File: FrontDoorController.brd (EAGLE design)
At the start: 31.4 x 52.1 mm, 2 parts

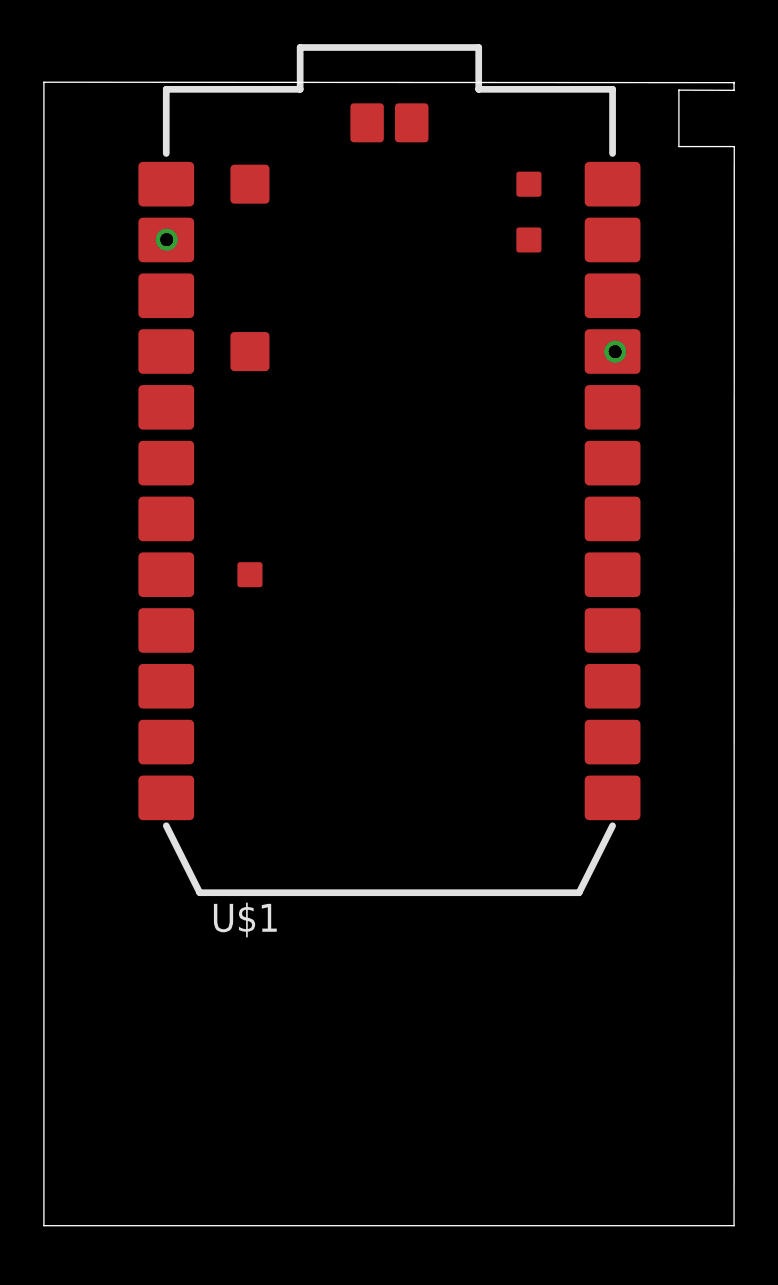
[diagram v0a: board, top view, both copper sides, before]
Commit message: Door_Control_PCB: Add motor driver and connect
Add the TB6612FNG motor driver and connect it to the Photon.  This will
take power from 4 AA batteries in the Lockitron and drive the Lockitron
motor.  The Photon will control direction and speed for the motor.
Since there is only 1 motor on the Lockitron, only 1 of the input/output
pairs on the driver needs to be connected.
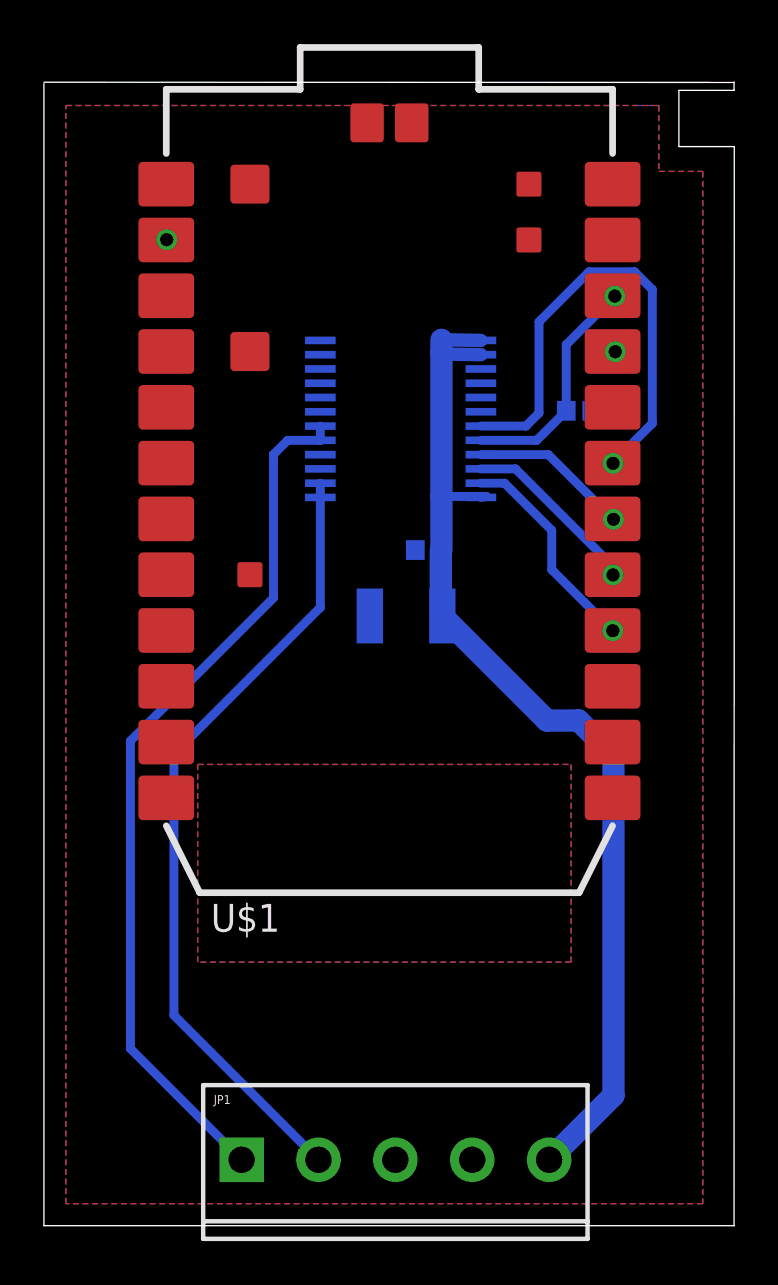
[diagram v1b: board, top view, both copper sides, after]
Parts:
- added C1: 10uf, SparkFun-Capacitors:EIA3528
- added C2, C3: 0.1uf, SparkFun-Capacitors:0402-CAP
- added JP1: (no value), SparkFun-Connectors:SCREWTERMINAL-3.5MM-5
- added U$2: TB6612FNG, SparkFun-PowerIC:SSOP24
- moved FRAME1 78.2 mm to (87.0, 34.0)
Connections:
- net RST_B renamed RSTB
- net SETUP_B renamed SETUPB
- removed net D3: U$1.16
- removed net D4: U$1.17
- removed net D5: U$1.18
- removed net D6: U$1.19
- removed net VBAT: U$1.22
- new net A01: JP1.2, U$2.1, U$2.2
- new net A02: JP1.1, U$2.5, U$2.6
- new net AIN1: U$1.18, U$2.21
- new net AIN2: U$1.17, U$2.22
- new net PWMA: U$1.16, U$2.23
- new net STBY: U$1.19, U$2.19
- new net VM: C1.A, C2.1, JP1.5, U$2.13, U$2.14, U$2.24
- net 3V3: now also C3.1, U$1.22, U$2.20
- net GND: now also C1.C, C2.2, C3.2, JP1.3, JP1.4, U$2.10, U$2.18, U$2.3, U$2.4, U$2.9
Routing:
- net VM: track 0.00 -> 48.6 mm
- net A02: track 0.00 -> 40.0 mm
- net A01: track 0.00 -> 36.3 mm
- net STBY: track 0.00 -> 22.2 mm, vias 0 -> 1
- net 3V3: track 0.00 -> 10.7 mm, vias 0 -> 1
- net PWMA: track 0.00 -> 9.82 mm, vias 0 -> 1
- net AIN2: track 0.00 -> 8.26 mm, vias 0 -> 1
- net AIN1: track 0.00 -> 7.25 mm, vias 0 -> 1
- net GND: track 0.00 -> 0.16 mm, vias 0 -> 2
- added copper zone on layer 1, net 3V3
- added copper zone on layer 16, net GND
- added copper zone on layer 1, net N$3
- added copper zone on layer 16, net N$4
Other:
- outline, holes or cut-outs redrawn
- board text added: "A01"
- board text added: "A02"
- board text added: "AAin"
- board text added: "GND"

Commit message: Door_Control_PCB: Add headers and diode
Exchange the screw terminals for 0.1" breakaway header holes.  There is
no room for the screw terminals in the Lockitron so wires will need to
be soldered directly to the board.  Some space can be saved by using
0.1" spacing header holes instead of the bigger pitch screw terminals.
Also do a few other minor cleanup tasks like change the size of the wire
input labels.  Also add a 1N4001 diode between VM from AA's and VIN on
Photon to drop the voltage from about 6V to about 5V to ensure it is
safe for the Photon VIN input.
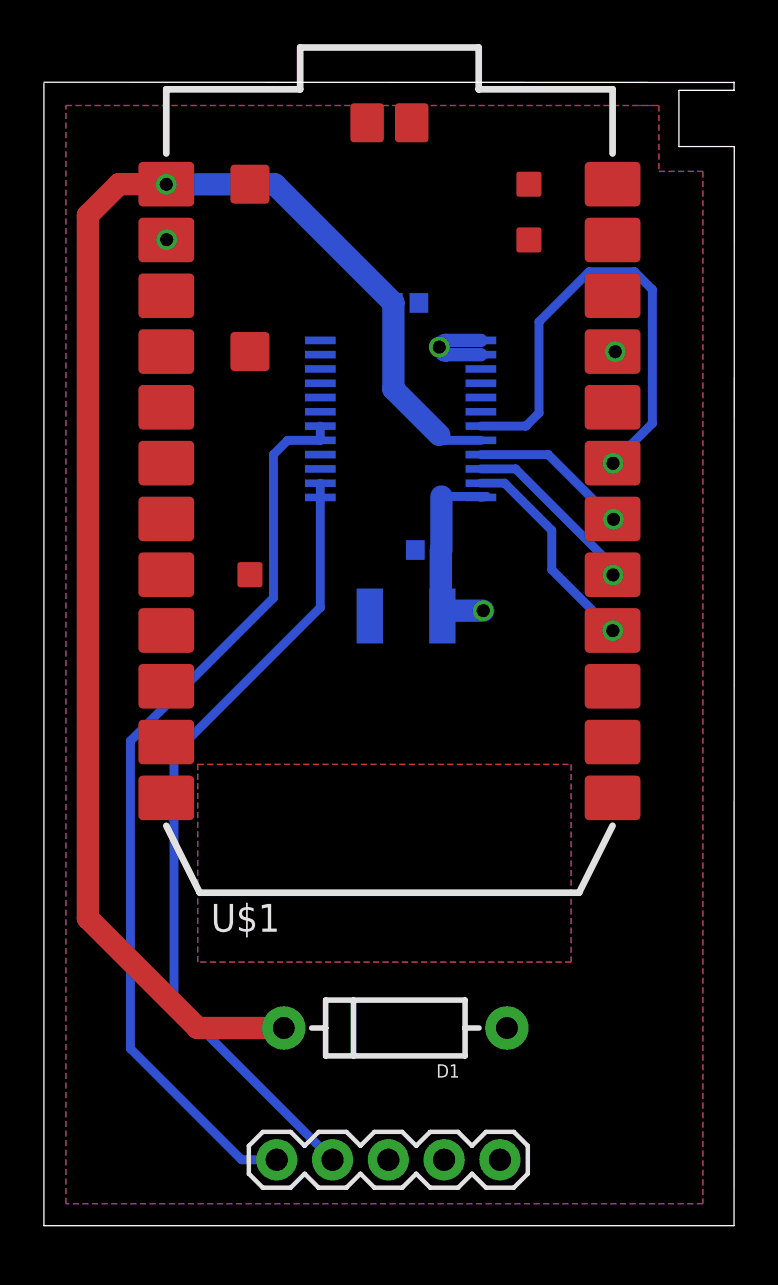
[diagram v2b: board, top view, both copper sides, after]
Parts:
- added D1: (no value), SparkFun-DiscreteSemi:DIODE-1N4001
- JP1: device SparkFun-Connectors:SCREWTERMINAL-3.5MM-5 -> SparkFun-Connectors:1X05
- moved C3 9.28 mm to (16.5, 42.0)
- moved JP1 1.60 mm to (10.6, 3.00)
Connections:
- new net VBAT: U$1.22
- net 3V3: no longer C3.1, U$1.22, U$2.20
- net VIN: now also C3.1, D1.C, U$2.20
- net VM: now also D1.A
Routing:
- net VIN: track 0.00 -> 68.6 mm, vias 0 -> 1
- net VM: track 48.6 -> 14.2 mm, vias 0 -> 2
- net 3V3: track 10.7 -> 0.00 mm, vias 1 -> 0
- net A02: track 40.0 -> 41.6 mm
- added copper zone on layer 1, net VM
- removed copper zone on layer 1, net 3V3
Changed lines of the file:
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@@
 <dimension x1="31.42" y1="51.69" x2="28.91" y2="51.7" x3="30.173240625" y3="53.763453125" textsize="1.778" layer="48" unit="inch"/>
 <dimension x1="31.42" y1="51.69" x2="31.43" y2="49.13" x3="39.882878125" y3="50.4430375" textsize="1.778" layer="48" unit="inch"/>
-<text x="10" y="7" size="1.778" layer="51" rot="R90">A02</text>
-<text x="13" y="7" size="1.778" layer="51" rot="R90">A01</text>
-<text x="15" y="7" size="1.778" layer="51">GND</text>
-<text x="24" y="7" size="1.778" layer="51" rot="R90">AAin</text>
+<text x="11" y="5" size="1.016" layer="51" rot="R90">A02</text>
+<text x="14" y="5" size="1.016" layer="51" rot="R90">A01</text>
+<text x="15.06" y="5" size="1.27" layer="51">GND</text>
+<text x="21" y="5" size="0.8128" layer="51" rot="R90">AAin</text>
 <wire x1="0" y1="0" x2="0" y2="52" width="0" layer="20"/>
 </plain>
@@
 <attribute name="NAME" x="17.719" y="31.5885" size="0.4064" layer="26" rot="MR0"/>
 </element>
-<element name="C3" library="SparkFun-Capacitors" package="0402-CAP" value="0.1uf" x="24.36" y="37.1" smashed="yes" rot="MR180">
-<attribute name="NAME" x="24.161" y="38.2315" size="0.4064" layer="26" rot="MR180"/>
+<element name="C3" library="SparkFun-Capacitors" package="0402-CAP" value="0.1uf" x="16.49" y="42.01" smashed="yes" rot="MR180">
+<attribute name="NAME" x="16.291" y="43.1415" size="0.4064" layer="26" rot="MR180"/>
 </element>
-<element name="JP1" library="SparkFun-Connectors" package="SCREWTERMINAL-3.5MM-5" value="" x="9" y="3">
-<attribute name="PROD_ID" value="Combine 8288+8399" x="9" y="3" size="1.778" layer="27" display="off"/>
+<element name="JP1" library="SparkFun-Connectors" package="1X05" value="" x="10.6" y="3" smashed="yes">
+<attribute name="VALUE" x="9.33" y="-0.175" size="1.27" layer="27"/>
 </element>
+<element name="D1" library="SparkFun-DiscreteSemi" package="DIODE-1N4001" value="" x="16" y="9" rot="R180"/>
 </elements>
 <signals>
 <signal name="VIN">
 <contactref element="U$1" pad="1"/>
+<contactref element="D1" pad="C"/>
+<wire x1="10.92" y1="9" x2="7" y2="9" width="1.016" layer="1"/>
+<wire x1="7" y1="9" x2="2" y2="14" width="1.016" layer="1"/>
+<wire x1="2" y1="14" x2="2" y2="46" width="1.016" layer="1"/>
+<wire x1="2" y1="46" x2="3.418" y2="47.418" width="1.016" layer="1"/>
+<wire x1="3.418" y1="47.418" x2="5.57" y2="47.418" width="1.016" layer="1"/>
+<contactref element="C3" pad="1"/>
+<contactref element="U$2" pad="20"/>
+<wire x1="15.91" y1="42.01" x2="15.91" y2="38.09" width="1.016" layer="16"/>
+<wire x1="15.91" y1="38.09" x2="18" y2="36" width="1.016" layer="16"/>
+<wire x1="18" y1="36" x2="18.245" y2="35.755" width="0.4064" layer="16"/>
+<wire x1="18.245" y1="35.755" x2="19.896" y2="35.755" width="0.4064" layer="16"/>
+<via x="5.57" y="47.41" extent="1-16" drill="0.6" shape="square"/>
+<wire x1="5.57" y1="47.41" x2="10.51" y2="47.41" width="1.016" layer="16"/>
+<wire x1="10.51" y1="47.41" x2="15.91" y2="42.01" width="1.016" layer="16"/>
+<wire x1="5.57" y1="47.418" x2="5.57" y2="47.41" width="0" layer="19" extent="1-1"/>
 </signal>
 <signal name="GND">
@@
 <signal name="3V3">
 <contactref element="U$1" pad="24"/>
-<contactref element="U$2" pad="20"/>
-<contactref element="U$1" pad="22"/>
-<contactref element="C3" pad="1"/>
-<polygon width="0.4064" layer="1">
-<vertex x="1" y="51"/>
-<vertex x="28" y="51"/>
-<vertex x="28" y="48"/>
-<vertex x="30" y="48"/>
-<vertex x="30" y="1"/>
-<vertex x="1" y="1"/>
-</polygon>
-<via x="25.99" y="42.32" extent="1-16" drill="0.6" shape="square"/>
-<wire x1="25.89" y1="42.338" x2="25.972" y2="42.338" width="0.4064" layer="16"/>
-<wire x1="25.972" y1="42.338" x2="25.99" y2="42.32" width="0.4064" layer="16"/>
-<wire x1="19.896" y1="35.755" x2="22.435" y2="35.755" width="0.4064" layer="16"/>
-<wire x1="22.435" y1="35.755" x2="23.78" y2="37.1" width="0.4064" layer="16"/>
-<wire x1="23.78" y1="37.1" x2="23.78" y2="40.11" width="0.4064" layer="16"/>
-<wire x1="23.78" y1="40.11" x2="25.99" y2="42.32" width="0.4064" layer="16"/>
 </signal>
 <signal name="RSTB">
@@
 <wire x1="12.584" y1="33.155" x2="12.584" y2="28.144" width="0.4064" layer="16"/>
 <wire x1="12.584" y1="28.144" x2="5.92" y2="21.48" width="0.4064" layer="16"/>
-<wire x1="5.92" y1="21.48" x2="5.92" y2="9.58" width="0.4064" layer="16"/>
-<wire x1="5.92" y1="9.58" x2="12.5" y2="3" width="0.4064" layer="16"/>
+<wire x1="13.14" y1="3" x2="5.92" y2="10.22" width="0.4064" layer="16"/>
+<wire x1="5.92" y1="10.22" x2="5.92" y2="21.48" width="0.4064" layer="16"/>
 </signal>
 <signal name="A02">
@@
 <wire x1="10.45" y1="28.58" x2="3.94" y2="22.07" width="0.4064" layer="16"/>
 <wire x1="3.94" y1="22.07" x2="3.94" y2="8.06" width="0.4064" layer="16"/>
-<wire x1="3.94" y1="8.06" x2="9" y2="3" width="0.4064" layer="16"/>
+<wire x1="10.6" y1="3" x2="9" y2="3" width="0.4064" layer="16"/>
+<wire x1="9" y1="3" x2="3.94" y2="8.06" width="0.4064" layer="16"/>
 </signal>
 <signal name="VM">
@@
 <wire x1="18.1" y1="33.2" x2="20.146" y2="33.2" width="0.4064" layer="16"/>
 <wire x1="20.146" y1="33.2" x2="19.896" y2="33.155" width="0.4064" layer="16"/>
-<wire x1="19.896" y1="40.305" x2="18.1" y2="40.335" width="0.6096" layer="16"/>
-<wire x1="18.1" y1="40.335" x2="18.1" y2="39.76" width="1.016" layer="16"/>
-<wire x1="18.1" y1="39.685" x2="18.1" y2="33.2" width="1.016" layer="16"/>
-<wire x1="19.896" y1="39.655" x2="18.1" y2="39.685" width="0.6096" layer="16"/>
 <wire x1="18.1" y1="39.685" x2="18.1" y2="39.76" width="0.4064" layer="16"/>
-<wire x1="18.14" y1="27.76" x2="22.9" y2="23" width="1.016" layer="16"/>
-<wire x1="22.9" y1="23" x2="24.34" y2="23" width="1.016" layer="16"/>
-<wire x1="24.34" y1="23" x2="25.93" y2="21.41" width="1.016" layer="16"/>
-<wire x1="25.93" y1="21.41" x2="25.93" y2="5.93" width="1.016" layer="16"/>
-<wire x1="25.93" y1="5.93" x2="23" y2="3" width="1.016" layer="16"/>
+<contactref element="D1" pad="A"/>
+<polygon width="0.4064" layer="1">
+<vertex x="1" y="51"/>
+<vertex x="28" y="51"/>
+<vertex x="28" y="48"/>
+<vertex x="30" y="48"/>
+<vertex x="30" y="1"/>
+<vertex x="1" y="1"/>
+</polygon>
+<wire x1="18.14" y1="27.76" x2="18.38" y2="28" width="1.016" layer="16"/>
+<wire x1="18.38" y1="28" x2="20" y2="28" width="1.016" layer="16"/>
+<via x="20" y="28" extent="1-16" drill="0.6"/>
+<via x="18" y="40" extent="1-16" drill="0.6"/>
+<wire x1="19.896" y1="40.305" x2="18.305" y2="40.305" width="0.6096" layer="16"/>
+<wire x1="18.305" y1="40.305" x2="18" y2="40" width="0.6096" layer="16" curve="90"/>
+<wire x1="19.896" y1="39.655" x2="18.345" y2="39.655" width="0.6096" layer="16"/>
+<wire x1="18.345" y1="39.655" x2="18" y2="40" width="0.6096" layer="16" curve="-90"/>
+<wire x1="18.345" y1="39.655" x2="18.205" y2="39.655" width="0.6096" layer="16"/>
+<wire x1="18.205" y1="39.655" x2="18.1" y2="39.76" width="0.6096" layer="16" curve="-90"/>
 </signal>
 <signal name="N$3">
@@
 <wire x1="25.89" y1="29.638" x2="25.89" y2="29.638" width="0" layer="19" extent="1-16"/>
 </signal>
+<signal name="VBAT">
+<contactref element="U$1" pad="22"/>
+</signal>
 </signals>

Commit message: Door_Control_PCB: Add Photon through holes
Add in an additional part for the Photon through-hole connections.  This
can be used to attach the Photon to the board without soldering it down.
Also reconnect the wires to the new Photon holes and clean up the
schematic a bit.
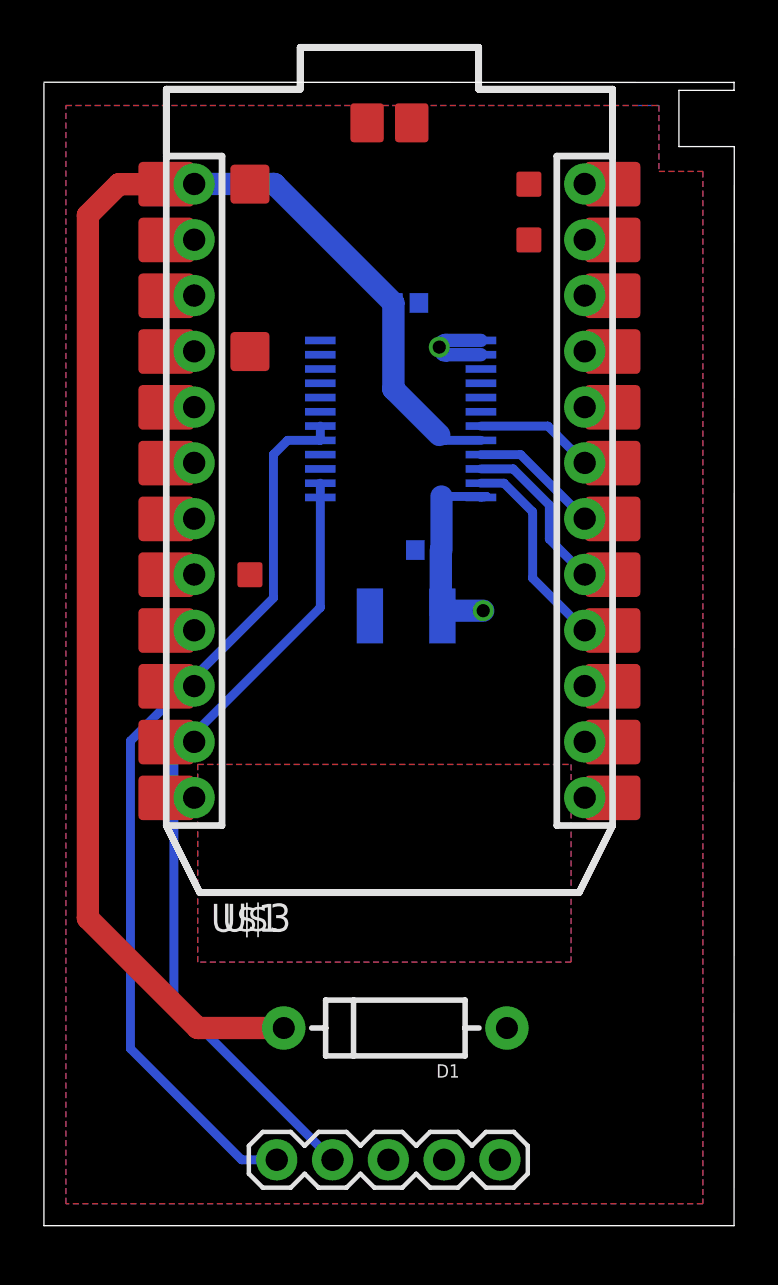
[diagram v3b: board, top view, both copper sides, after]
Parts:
- added U$3: PHOTON_WITH_HEADERS, Spark:PHOTON
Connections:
- net 3V3: now also U$3.24
- net A0: now also U$3.12
- net A1: now also U$3.11
- net A2: now also U$3.10
- net A3: now also U$3.9
- net A4: now also U$3.8
- net A5: now also U$3.7
- net AIN1: now also U$3.18
- net AIN2: now also U$3.17
- net D0: now also U$3.13
- net D1: now also U$3.14
- net D2: now also U$3.15
- net D7: now also U$3.20
- net DAC: now also U$3.6
- net GND: now also U$3.2, U$3.21
- net PWMA: now also U$3.16
- net RSTB: now also U$3.23
- net RX: now also U$3.4
- net STBY: now also U$3.19
- net TX: now also U$3.3
- net VBAT: now also U$3.22
- net VIN: now also U$3.1
- net WKP: now also U$3.5
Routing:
- net STBY: track 22.2 -> 6.69 mm, vias 1 -> 0
- net GND: track 0.16 -> 2.69 mm, vias 2 -> 0
- net A5: track 0.00 -> 1.27 mm
- net A3: track 0.00 -> 1.27 mm
- net A2: track 0.00 -> 1.27 mm
- net D2: track 0.00 -> 1.27 mm
- net VBAT: track 0.00 -> 1.27 mm
- net RSTB: track 0.00 -> 1.27 mm
- net D7: track 0.00 -> 1.27 mm
- net 3V3: track 0.00 -> 1.27 mm
- net WKP: track 0.00 -> 1.27 mm
- net TX: track 0.00 -> 1.27 mm
- net RX: track 0.00 -> 1.27 mm
- net DAC: track 0.00 -> 1.27 mm
- net A4: track 0.00 -> 1.27 mm
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
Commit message: Door_Control_PCB: Shrink the board a bit to save money
The board did not need to be nearly as big as it was and shrinking it a
bit can save some money in maunfacturing.
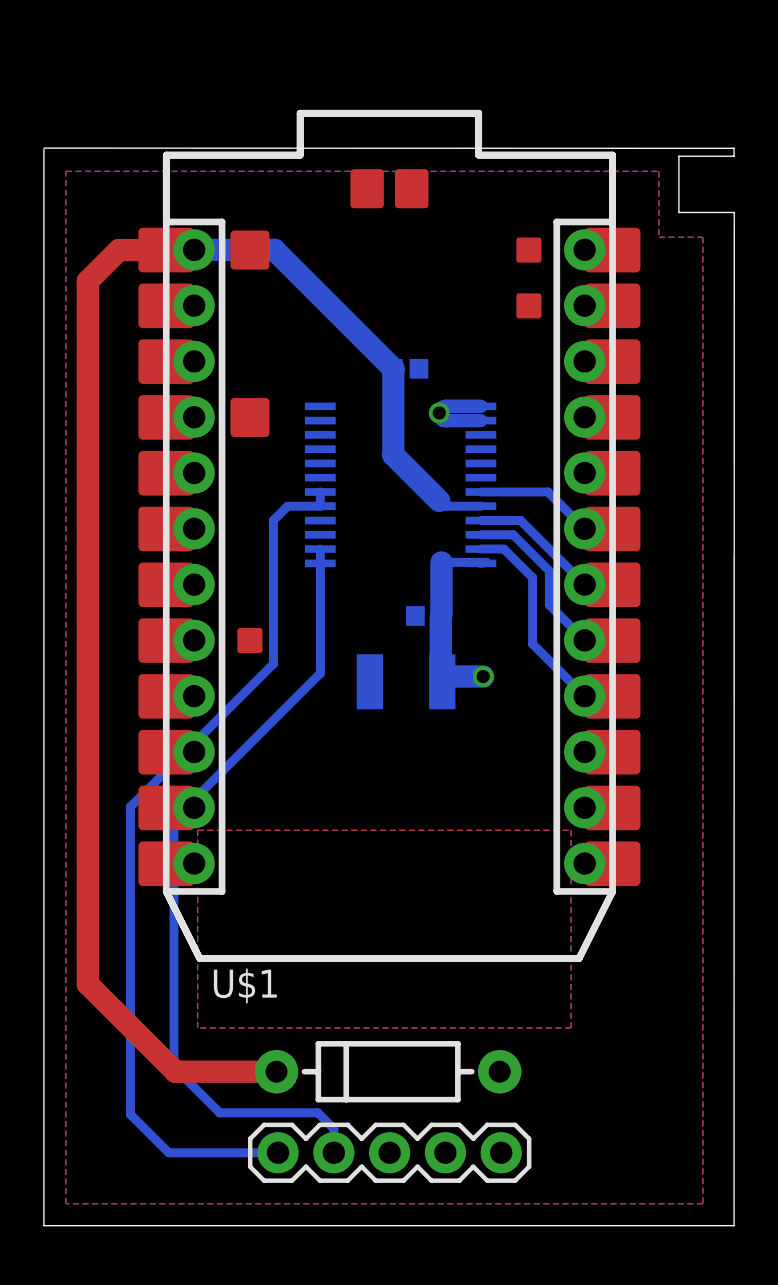
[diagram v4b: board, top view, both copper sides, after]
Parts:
- moved C1 3.00 mm to (16.5, 24.8)
- moved C2 3.00 mm to (17.5, 27.8)
- moved C3 3.00 mm to (16.5, 39.0)
- moved U$1 3.00 mm to (5.57, 12.2)
- moved U$2 3.00 mm to (16.2, 33.7)
- moved U$3 3.00 mm to (5.57, 12.2)
- moved D1 2.02 mm to (15.7, 7.01)
- moved JP1 0.33 mm to (10.7, 3.32)
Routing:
- net A02: track 41.6 -> 40.2 mm
- net VIN: track 68.6 -> 67.9 mm
- net A01: track 36.6 -> 35.9 mm
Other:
- board size 31.4 x 52.1 mm -> 31.4 x 49.1 mm
- board text removed: "A01"
- board text removed: "A02"
- board text removed: "AAin"
- board text removed: "GND"
